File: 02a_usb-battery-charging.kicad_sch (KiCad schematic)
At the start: 20 parts, among them J1 USB4105-GF-A, J3 Conn_01x03_Socket, J8 Conn_01x02_Socket, U1 NUP3115UPMUTAG, U2 BQ25170JDSGR

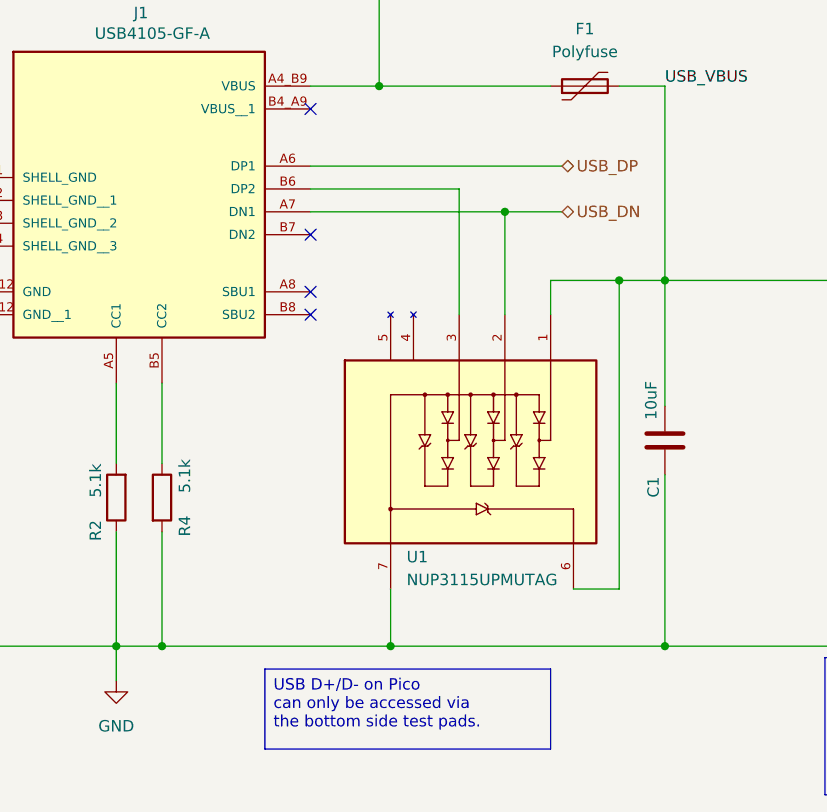
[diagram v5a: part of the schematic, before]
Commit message: better integration for the USB ESD diodes, better trace length matching
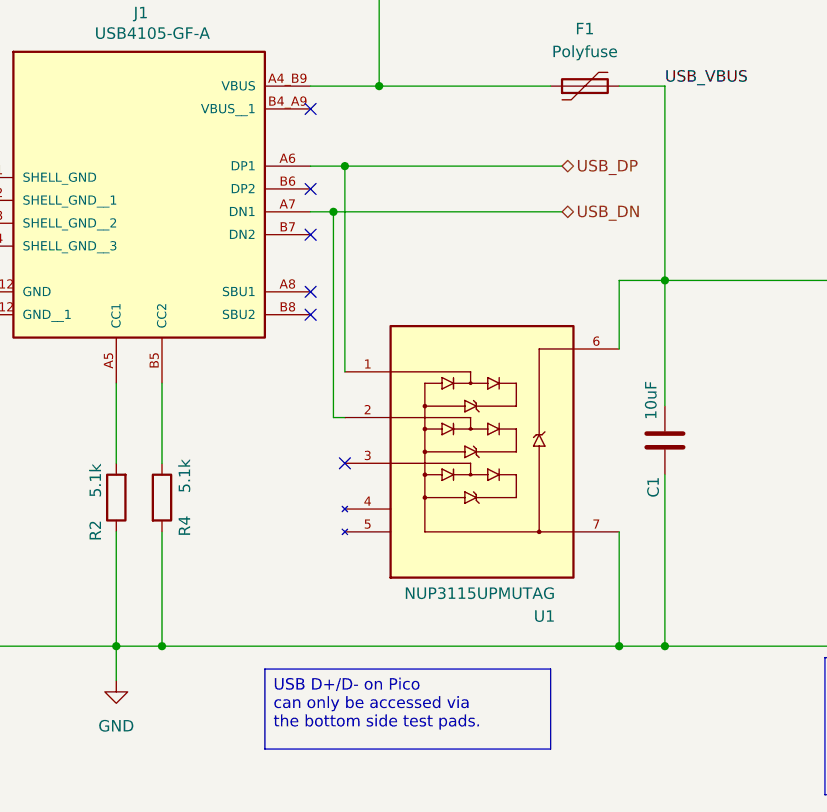
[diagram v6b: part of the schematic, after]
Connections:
- net USB_DP: now also U1.1
- net USB_VBUS: no longer U1.1
- net at U1.3: no longer J1.B6 (DP2)
- no-connect marks 6 -> 8
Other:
- moved on the sheet: U1
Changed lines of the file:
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@@
+	)
+	(junction
+		(at 71.12 68.58)
+		(diameter 0)
+		(color 0 0 0 0)
 	)
 	(junction
@@
 	)
 	(junction
-		(at 90.17 68.58)
+		(at 72.39 63.5)
 		(diameter 0)
 		(color 0 0 0 0)
@@
 	)
 	(junction
-		(at 77.47 116.84)
+		(at 102.87 116.84)
 		(diameter 0)
 		(color 0 0 0 0)
@@
 	)
 	(junction
-		(at 102.87 76.2)
-		(diameter 0)
-		(color 0 0 0 0)
-	)
-	(junction
 		(at 76.2 41.91)
 		(diameter 0)
 		(color 0 0 0 0)
+	)
+	(no_connect
+		(at 68.58 66.04)
 	)
 	(no_connect
@@
 	)
 	(no_connect
+		(at 72.39 96.52)
+	)
+	(no_connect
 		(at 154.94 182.88)
 	)
@@
 	(wire
 		(pts
-			(xy 90.17 68.58) (xy 90.17 80.01)
-		)
-		(stroke
-			(width 0)
-			(type default)
-		)
-	)
-	(wire
-		(pts
-			(xy 85.09 66.04) (xy 85.09 80.01)
+			(xy 71.12 68.58) (xy 71.12 91.44)
 		)
 		(stroke
@@
 	(wire
 		(pts
-			(xy 77.47 110.49) (xy 77.47 116.84)
-		)
-		(stroke
-			(width 0)
-			(type default)
-		)
-	)
-	(wire
-		(pts
 			(xy 147.32 99.06) (xy 149.86 99.06)
 		)
@@
 	(wire
 		(pts
+			(xy 72.39 86.36) (xy 72.39 63.5)
+		)
+		(stroke
+			(width 0)
+			(type default)
+		)
+	)
+	(wire
+		(pts
 			(xy 29.21 80.01) (xy 30.48 80.01)
 		)
@@
 	(wire
 		(pts
+			(xy 102.87 116.84) (xy 107.95 116.84)
+		)
+		(stroke
+			(width 0)
+			(type default)
+		)
+	)
+	(wire
+		(pts
 			(xy 40.64 187.96) (xy 44.45 187.96)
 		)
@@
 	(wire
 		(pts
-			(xy 77.47 116.84) (xy 107.95 116.84)
+			(xy 52.07 116.84) (xy 102.87 116.84)
 		)
 		(stroke
@@
 	(wire
 		(pts
-			(xy 95.25 80.01) (xy 95.25 76.2)
-		)
-		(stroke
-			(width 0)
-			(type default)
-		)
-	)
-	(wire
-		(pts
 			(xy 147.32 99.06) (xy 147.32 116.84)
 		)
@@
 	(wire
 		(pts
-			(xy 95.25 76.2) (xy 102.87 76.2)
-		)
-		(stroke
-			(width 0)
-			(type default)
-		)
-	)
-	(wire
-		(pts
-			(xy 68.58 63.5) (xy 96.52 63.5)
+			(xy 68.58 63.5) (xy 72.39 63.5)
 		)
 		(stroke
@@
 	(wire
 		(pts
+			(xy 102.87 83.82) (xy 102.87 76.2)
+		)
+		(stroke
+			(width 0)
+			(type default)
+		)
+	)
+	(wire
+		(pts
 			(xy 46.99 87.63) (xy 46.99 96.52)
 		)
@@
 	(wire
 		(pts
-			(xy 52.07 116.84) (xy 77.47 116.84)
-		)
-		(stroke
-			(width 0)
-			(type default)
-		)
-	)
-	(wire
-		(pts
 			(xy 190.5 74.93) (xy 190.5 76.2)
 		)
@@
 	(wire
 		(pts
-			(xy 97.79 110.49) (xy 102.87 110.49)
+			(xy 71.12 91.44) (xy 72.39 91.44)
 		)
 		(stroke
@@
 	(wire
 		(pts
+			(xy 71.12 68.58) (xy 96.52 68.58)
+		)
+		(stroke
+			(width 0)
+			(type default)
+		)
+	)
+	(wire
+		(pts
 			(xy 76.2 54.61) (xy 95.25 54.61)
 		)
@@
 	(wire
 		(pts
-			(xy 68.58 66.04) (xy 85.09 66.04)
-		)
-		(stroke
-			(width 0)
-			(type default)
-		)
-	)
-	(wire
-		(pts
 			(xy 29.21 72.39) (xy 30.48 72.39)
 		)
@@
 	(wire
 		(pts
-			(xy 68.58 68.58) (xy 90.17 68.58)
+			(xy 68.58 68.58) (xy 71.12 68.58)
 		)
 		(stroke
@@
 	(wire
 		(pts
-			(xy 90.17 68.58) (xy 96.52 68.58)
-		)
-		(stroke
-			(width 0)
-			(type default)
-		)
-	)
-	(wire
-		(pts
 			(xy 132.08 116.84) (xy 139.7 116.84)
 		)
@@
 	(wire
 		(pts
+			(xy 72.39 63.5) (xy 96.52 63.5)
+		)
+		(stroke
+			(width 0)
+			(type default)
+		)
+	)
+	(wire
+		(pts
 			(xy 187.96 83.82) (xy 190.5 83.82)
 		)
@@
 	(wire
 		(pts
-			(xy 102.87 110.49) (xy 102.87 76.2)
+			(xy 102.87 116.84) (xy 102.87 104.14)
 		)
 		(stroke
@@
 	(symbol
 		(lib_id "NUP3115UPMUTAG:NUP3115UPMUTAG")
-		(at 87.63 95.25 270)
+		(at 87.63 93.98 0)
 		(unit 1)
 		(exclude_from_sim no)
@@
 		(dnp no)
 		(property "Reference" "U1"
-			(at 79.248 106.934 90)
-			(effects
-				(font
-					(size 1.27 1.27)
-				)
-				(justify left)
+			(at 95.758 113.538 0)
+			(effects
+				(font
+					(size 1.27 1.27)
+				)
+				(justify right)
 			)
 		)
 		(property "Value" "NUP3115UPMUTAG"
-			(at 79.248 109.474 90)
-			(effects
-				(font
-					(size 1.27 1.27)
-				)
-				(justify left)
+			(at 95.758 110.998 0)
+			(effects
+				(font
+					(size 1.27 1.27)
+				)
+				(justify right)
 			)
 		)
 		(property "Footprint" "prj-footprints:UDFN6_1P60X1P60_ONS"
-			(at 87.63 95.25 0)
+			(at 87.63 93.98 0)
 			(effects
 				(font
@@
 		)
 		(property "Datasheet" ""
-			(at 87.63 95.25 0)
+			(at 87.63 93.98 0)
 			(effects
 				(font
@@
 		)
 		(property "Description" ""
-			(at 87.63 95.25 0)
+			(at 87.63 93.98 0)
 			(effects
 				(font
@@
 		)
 		(property "PARTREV" "Rev. 3"
-			(at 87.63 95.25 0)
+			(at 87.63 93.98 0)
 			(effects
 				(font
@@
 		)
 		(property "SNAPEDA_PN" "NUP3115UPMUTAG"
-			(at 87.63 95.25 0)
+			(at 87.63 93.98 0)
 			(effects
 				(font
@@
 		)
 		(property "MANUFACTURER" "Onsemi"
-			(at 87.63 95.25 0)
+			(at 87.63 93.98 0)
 			(effects
 				(font
@@
 		)
 		(property "MAXIMUM_PACKAGE_HEIGHT" "0.55 mm"
-			(at 87.63 95.25 0)
+			(at 87.63 93.98 0)
 			(effects
 				(font
@@
 		)
 		(property "STANDARD" "IPC 7351B"
-			(at 87.63 95.25 0)
-			(effects
-				(font
+			(at 87.63 93.98 0)
+			(effects
+				(font

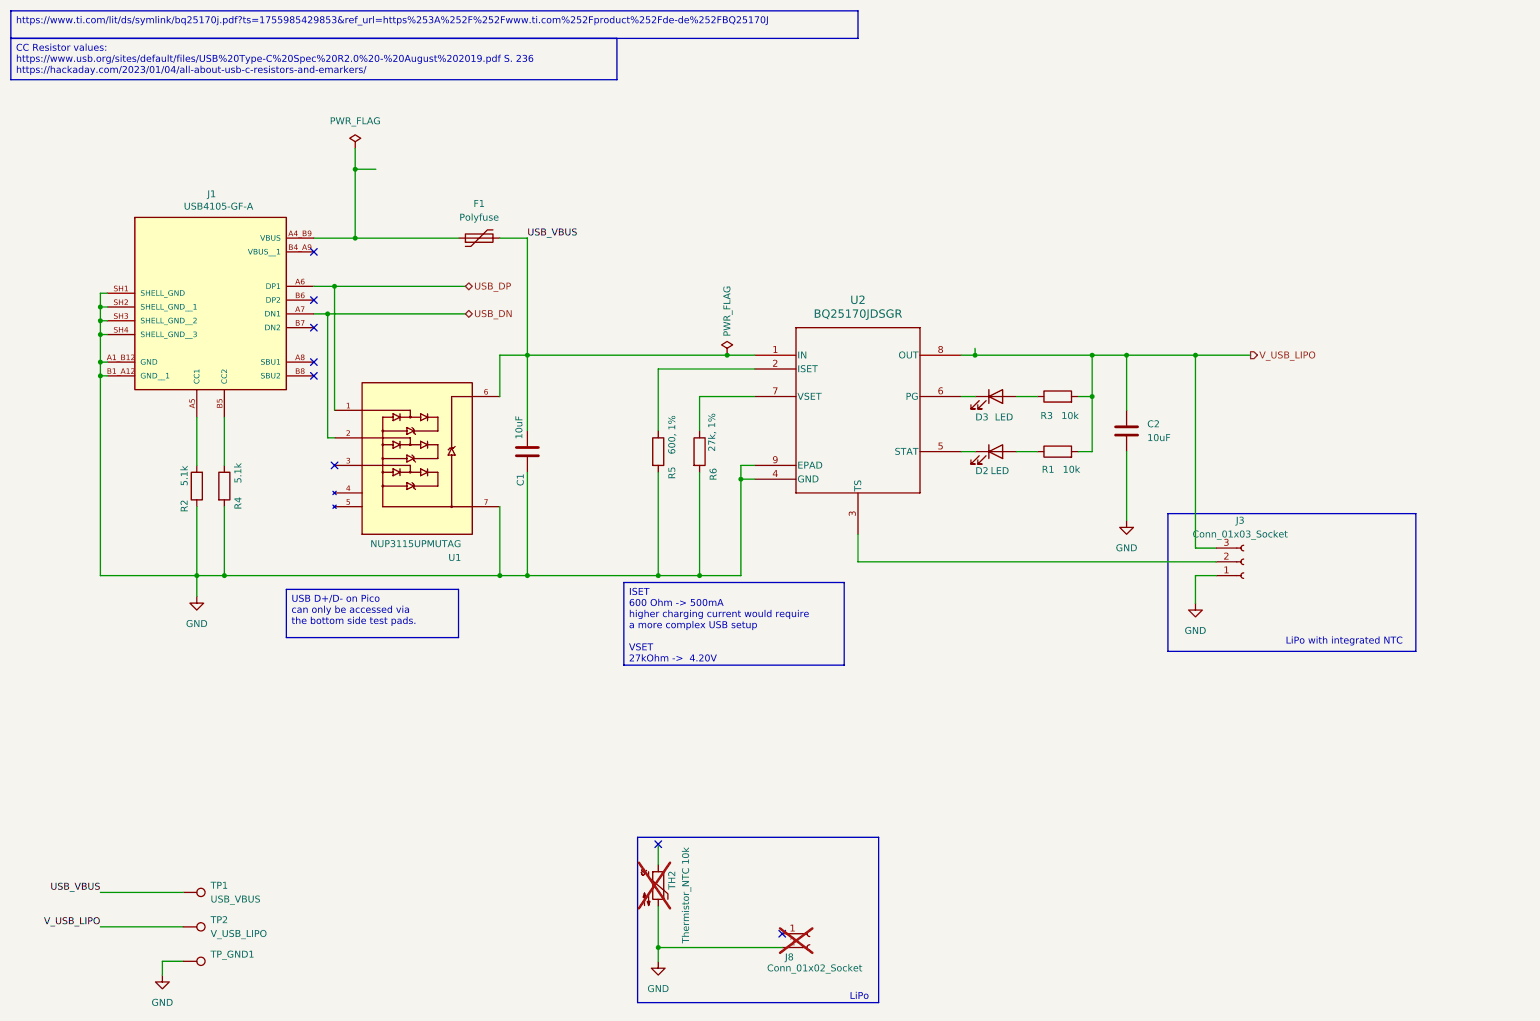
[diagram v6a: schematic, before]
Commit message: Connect both USB data lines again, checked everything with datasheets again
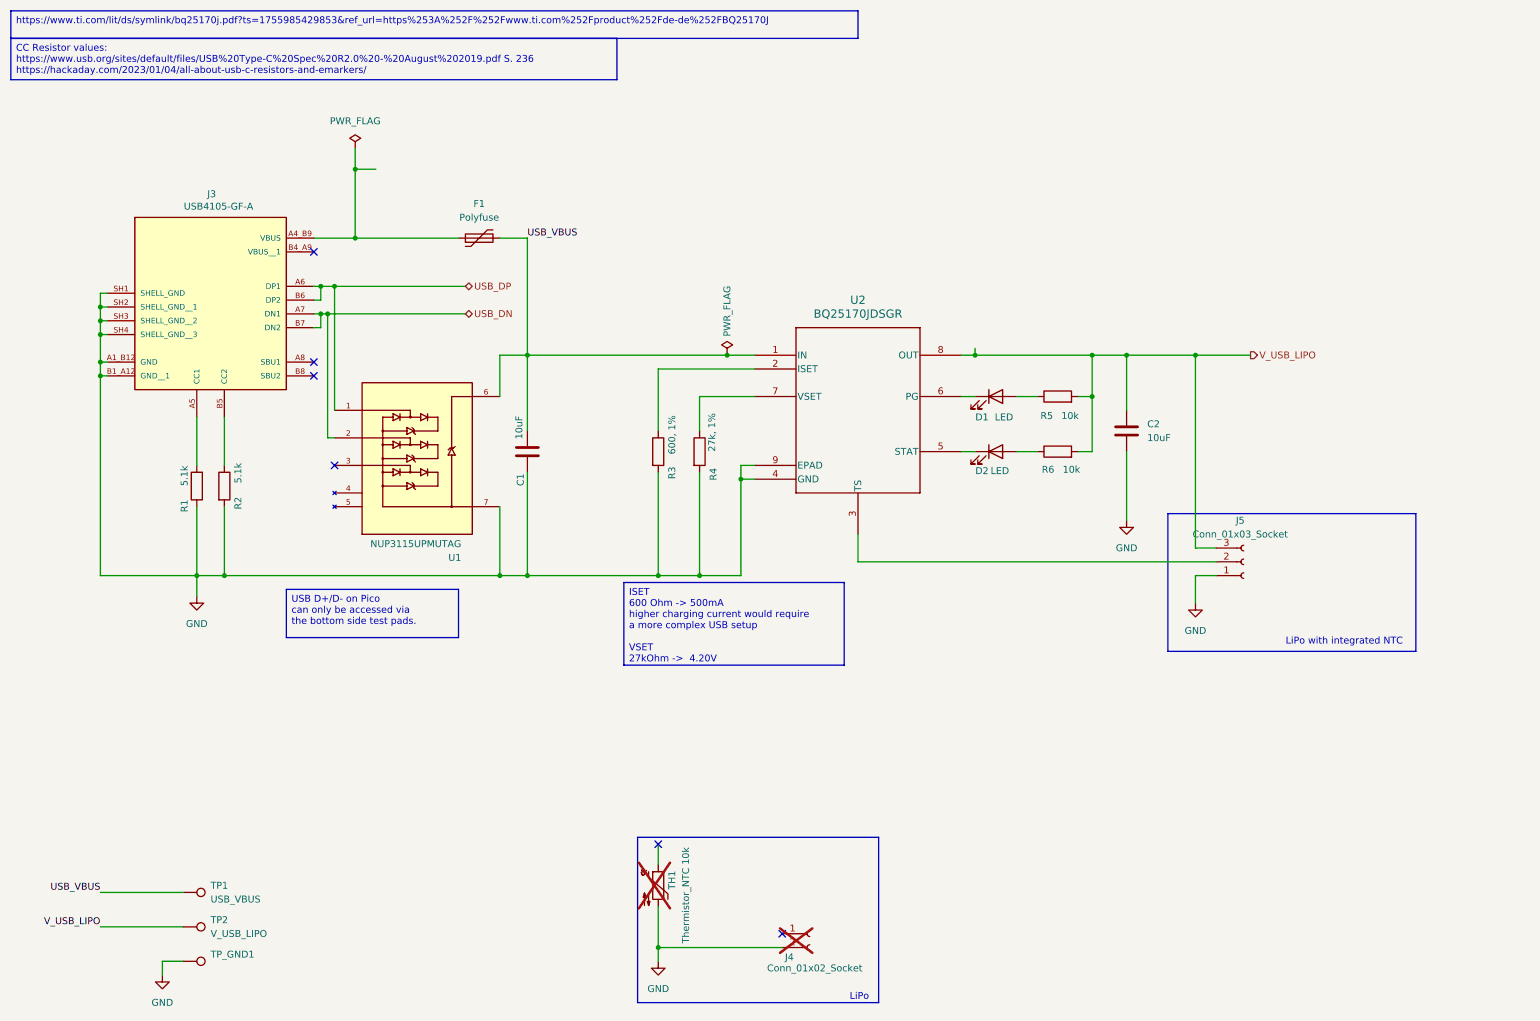
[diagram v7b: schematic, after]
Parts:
- renumbered D3 to D1, J1 to J3, J8 to J4, J3 to J5, R2 to R1, R4 to R2, R5 to R3, R6 to R4, R3 to R5, R1 to R6, TH2 to TH1
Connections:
- net USB_DN: now also J3.B7 (DN2)
- net USB_DP: now also J3.B6 (DP2)
- no-connect marks 8 -> 6
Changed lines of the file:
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@@
+	)
+	(junction
+		(at 69.85 68.58)
+		(diameter 0)
+		(color 0 0 0 0)
 	)
 	(junction
@@
 	)
 	(junction
+		(at 69.85 63.5)
+		(diameter 0)
+		(color 0 0 0 0)
+	)
+	(junction
 		(at 76.2 41.91)
 		(diameter 0)
@@
 	)
 	(no_connect
-		(at 68.58 66.04)
-	)
-	(no_connect
 		(at 68.58 57.15)
 	)
@@
 	)
 	(no_connect
-		(at 68.58 71.12)
-	)
-	(no_connect
 		(at 132.08 166.37)
 	)
@@
 	(wire
 		(pts
+			(xy 68.58 71.12) (xy 69.85 71.12)
+		)
+		(stroke
+			(width 0)
+			(type default)
+		)
+	)
+	(wire
+		(pts
 			(xy 212.09 76.2) (xy 218.44 76.2)
 		)
@@
 	(wire
 		(pts
+			(xy 68.58 66.04) (xy 69.85 66.04)
+		)
+		(stroke
+			(width 0)
+			(type default)
+		)
+	)
+	(wire
+		(pts
 			(xy 149.86 96.52) (xy 147.32 96.52)
 		)
@@
 	(wire
 		(pts
+			(xy 69.85 63.5) (xy 72.39 63.5)
+		)
+		(stroke
+			(width 0)
+			(type default)
+		)
+	)
+	(wire
+		(pts
 			(xy 107.95 76.2) (xy 144.78 76.2)
 		)
@@
 	(wire
 		(pts
+			(xy 69.85 66.04) (xy 69.85 63.5)
+		)
+		(stroke
+			(width 0)
+			(type default)
+		)
+	)
+	(wire
+		(pts
 			(xy 212.09 76.2) (xy 212.09 83.82)
 		)
@@
 	(wire
 		(pts
+			(xy 69.85 68.58) (xy 71.12 68.58)
+		)
+		(stroke
+			(width 0)
+			(type default)
+		)
+	)
+	(wire
+		(pts
 			(xy 231.14 116.84) (xy 231.14 121.92)
 		)
@@
 	(wire
 		(pts
-			(xy 68.58 63.5) (xy 72.39 63.5)
+			(xy 68.58 63.5) (xy 69.85 63.5)
 		)
 		(stroke
@@
 	(wire
 		(pts
+			(xy 69.85 71.12) (xy 69.85 68.58)
+		)
+		(stroke
+			(width 0)
+			(type default)
+		)
+	)
+	(wire
+		(pts
 			(xy 29.21 72.39) (xy 30.48 72.39)
 		)
@@
 	(wire
 		(pts
-			(xy 68.58 68.58) (xy 71.12 68.58)
+			(xy 68.58 68.58) (xy 69.85 68.58)
 		)
 		(stroke
@@
 		(on_board yes)
 		(dnp no)
-		(property "Reference" "D3"
+		(property "Reference" "D1"
 			(at 191.77 87.63 0)
 			(effects
@@
 			(project "ZEReader-Pico"
 				(path "/ec954637-2a8b-4662-b4a1-f88107f11cb0/a18230d5-251f-4044-a9cd-045093d87cd6"
-					(reference "D3")
+					(reference "D1")
 					(unit 1)
 				)
@@
 		(on_board no)
 		(dnp yes)
-		(property "Reference" "J8"
+		(property "Reference" "J4"
 			(at 155.448 187.198 0)
 			(effects
@@
 			(project "ZEReader-Pico"
 				(path "/ec954637-2a8b-4662-b4a1-f88107f11cb0/a18230d5-251f-4044-a9cd-045093d87cd6"
-					(reference "J8")
+					(reference "J4")
 					(unit 1)
 				)
@@
 		(on_board yes)
 		(dnp no)
-		(property "Reference" "R2"
+		(property "Reference" "R1"
 			(at 44.704 105.156 90)
 			(effects
@@
 			(project "ZEReader-Pico"
 				(path "/ec954637-2a8b-4662-b4a1-f88107f11cb0/a18230d5-251f-4044-a9cd-045093d87cd6"
-					(reference "R2")
+					(reference "R1")
 					(unit 1)
 				)
@@
 		(on_board no)
 		(dnp yes)
-		(property "Reference" "TH2"
+		(property "Reference" "TH1"
 			(at 134.62 174.752 90)
 			(effects
@@
 			(project "ZEReader-Pico"
 				(path "/ec954637-2a8b-4662-b4a1-f88107f11cb0/a18230d5-251f-4044-a9cd-045093d87cd6"
-					(reference "TH2")
+					(reference "TH1")
 					(unit 1)
 				)
@@
 			)
 		)
-		(property "Datasheet" "~"
+		(property "Datasheet" "https://www.digikey.de/de/products/detail/littelfuse-inc/1206L050-15YR/1211396"
 			(at 99.06 54.61 0)
 			(effects
@@
 		(on_board yes)
 		(dnp no)
-		(property "Reference" "J3"
+		(property "Reference" "J5"
 			(at 239.395 106.68 0)
 			(effects
@@
 			(project ""
 				(path "/ec954637-2a8b-4662-b4a1-f88107f11cb0/a18230d5-251f-4044-a9cd-045093d87cd6"
-					(reference "J3")
+					(reference "J5")
 					(unit 1)
 				)
@@
 		(on_board yes)
 		(dnp no)
-		(property "Reference" "R6"
+		(property "Reference" "R4"
 			(at 142.24 99.314 90)
 			(effects
@@
 			(project "ZEReader-Pico"
 				(path "/ec954637-2a8b-4662-b4a1-f88107f11cb0/a18230d5-251f-4044-a9cd-045093d87cd6"
-					(reference "R6")
+					(reference "R4")
 					(unit 1)
 				)
@@
 		(dnp no)
 		(fields_autoplaced yes)
-		(property "Reference" "#PWR017"
+		(property "Reference" "#PWR011"
 			(at 132.08 194.31 0)
 			(effects
@@
 			(project "ZEReader-Pico"
 				(path "/ec954637-2a8b-4662-b4a1-f88107f11cb0/a18230d5-251f-4044-a9cd-045093d87cd6"
-					(reference "#PWR017")
+					(reference "#PWR011")
 					(unit 1)
 				)
@@
 		(on_board yes)
 		(dnp no)
-		(property "Reference" "R1"
+		(property "Reference" "R6"
 			(at 203.962 97.282 90)
 			(effects
@@
 			(project "ZEReader-Pico"
 				(path "/ec954637-2a8b-4662-b4a1-f88107f11cb0/a18230d5-251f-4044-a9cd-045093d87cd6"
-					(reference "R1")
+					(reference "R6")
 					(unit 1)
 				)
@@
 		(on_board yes)
 		(dnp no)
-		(property "Reference" "#FLG03"
+		(property "Reference" "#FLG02"
 			(at 144.78 74.295 0)
 			(effects
@@
 			(project "ZEReader-Pico"
 				(path "/ec954637-2a8b-4662-b4a1-f88107f11cb0/a18230d5-251f-4044-a9cd-045093d87cd6"
-					(reference "#FLG03")
+					(reference "#FLG02")
 					(unit 1)
 				)
@@
 		(dnp no)
 		(fields_autoplaced yes)
-		(property "Reference" "#FLG04"
+		(property "Reference" "#FLG01"
 			(at 76.2 36.195 0)
 			(effects
@@
 			(project "ZEReader-Pico"
 				(path "/ec954637-2a8b-4662-b4a1-f88107f11cb0/a18230d5-251f-4044-a9cd-045093d87cd6"
-					(reference "#FLG04")
+					(reference "#FLG01")
 					(unit 1)
 				)
@@
 		(on_board yes)
 		(dnp no)
-		(property "Reference" "R5"
+		(property "Reference" "R3"
 			(at 134.62 99.06 90)
 			(effects
@@
 			(project "ZEReader-Pico"
 				(path "/ec954637-2a8b-4662-b4a1-f88107f11cb0/a18230d5-251f-4044-a9cd-045093d87cd6"
-					(reference "R5")
+					(reference "R3")
 					(unit 1)
 				)
@@
 		(on_board yes)
 		(dnp no)
-		(property "Reference" "#PWR018"
+		(property "Reference" "#PWR012"
 			(at 218.44 113.03 0)
 			(effects
@@
 			(project "ZEReader-Pico"
 				(path "/ec954637-2a8b-4662-b4a1-f88107f11cb0/a18230d5-251f-4044-a9cd-045093d87cd6"
-					(reference "#PWR018")
+					(reference "#PWR012")
 					(unit 1)
 				)
@@
 		(on_board yes)
 		(dnp no)
-		(property "Reference" "#PWR024"
+		(property "Reference" "#PWR013"
 			(at 231.14 128.27 0)
 			(effects
@@
 			(project "ZEReader-Pico"
 				(path "/ec954637-2a8b-4662-b4a1-f88107f11cb0/a18230d5-251f-4044-a9cd-045093d87cd6"
-					(reference "#PWR024")
+					(reference "#PWR013")
 					(unit 1)
 				)
@@
 		(on_board yes)
 		(dnp no)
-		(property "Reference" "J1"
+		(property "Reference" "J3"
 			(at 50.546 46.482 0)
 			(effects
@@
 			(project "ZEReader-Pico"
 				(path "/ec954637-2a8b-4662-b4a1-f88107f11cb0/a18230d5-251f-4044-a9cd-045093d87cd6"
-					(reference "J1")
+					(reference "J3")
 					(unit 1)
 				)
@@
 		(on_board yes)
 		(dnp no)
-		(property "Reference" "R4"
+		(property "Reference" "R2"
 			(at 54.61 104.648 90)
 			(effects
@@
 			(project "ZEReader-Pico"
 				(path "/ec954637-2a8b-4662-b4a1-f88107f11cb0/a18230d5-251f-4044-a9cd-045093d87cd6"
-					(reference "R4")
+					(reference "R2")
 					(unit 1)
 				)
@@
 		(dnp no)
 		(fields_autoplaced yes)
-		(property "Reference" "#PWR016"
+		(property "Reference" "#PWR010"
 			(at 46.99 127 0)
 			(effects
@@
 			(project "ZEReader-Pico"
 				(path "/ec954637-2a8b-4662-b4a1-f88107f11cb0/a18230d5-251f-4044-a9cd-045093d87cd6"
-					(reference "#PWR016")
+					(reference "#PWR010")
 					(unit 1)
 				)
@@
 		(dnp no)
 		(fields_autoplaced yes)
-		(property "Reference" "#PWR015"
+		(property "Reference" "#PWR09"
 			(at 40.64 196.85 0)
 			(effects
@@
 			(project ""
 				(path "/ec954637-2a8b-4662-b4a1-f88107f11cb0/a18230d5-251f-4044-a9cd-045093d87cd6"
-					(reference "#PWR015")
+					(reference "#PWR09")
 					(unit 1)
 				)
@@
 		(on_board yes)
 		(dnp no)
-		(property "Reference" "R3"
+		(property "Reference" "R5"
 			(at 203.708 87.376 90)
 			(effects
@@
 			(project "ZEReader-Pico"
 				(path "/ec954637-2a8b-4662-b4a1-f88107f11cb0/a18230d5-251f-4044-a9cd-045093d87cd6"
-					(reference "R3")
+					(reference "R5")
 					(unit 1)
 				)

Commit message: Reworked the PCB after review
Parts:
- removed U1: NUP3115UPMUTAG, prj-footprints:UDFN6_1P60X1P60_ONS, symbol NUP3115UPMUTAG:NUP3115UPMUTAG
- added U1: USBLC6-2SC6, Package_TO_SOT_SMD:SOT-23-6, symbol Power_Protection:USBLC6-2SC6
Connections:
- net GND: now also U1.2 (GND)
- net USB_DN: now also U1.3 (I/O2)
- net USB_DP: now also U1.1 (I/O1)
- net USB_VBUS: now also U1.5 (VBUS)
- no-connect marks 6 -> 7
